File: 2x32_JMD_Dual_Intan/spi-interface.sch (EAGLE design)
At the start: 40 parts, among them Q1 BC817, Q2 BC817

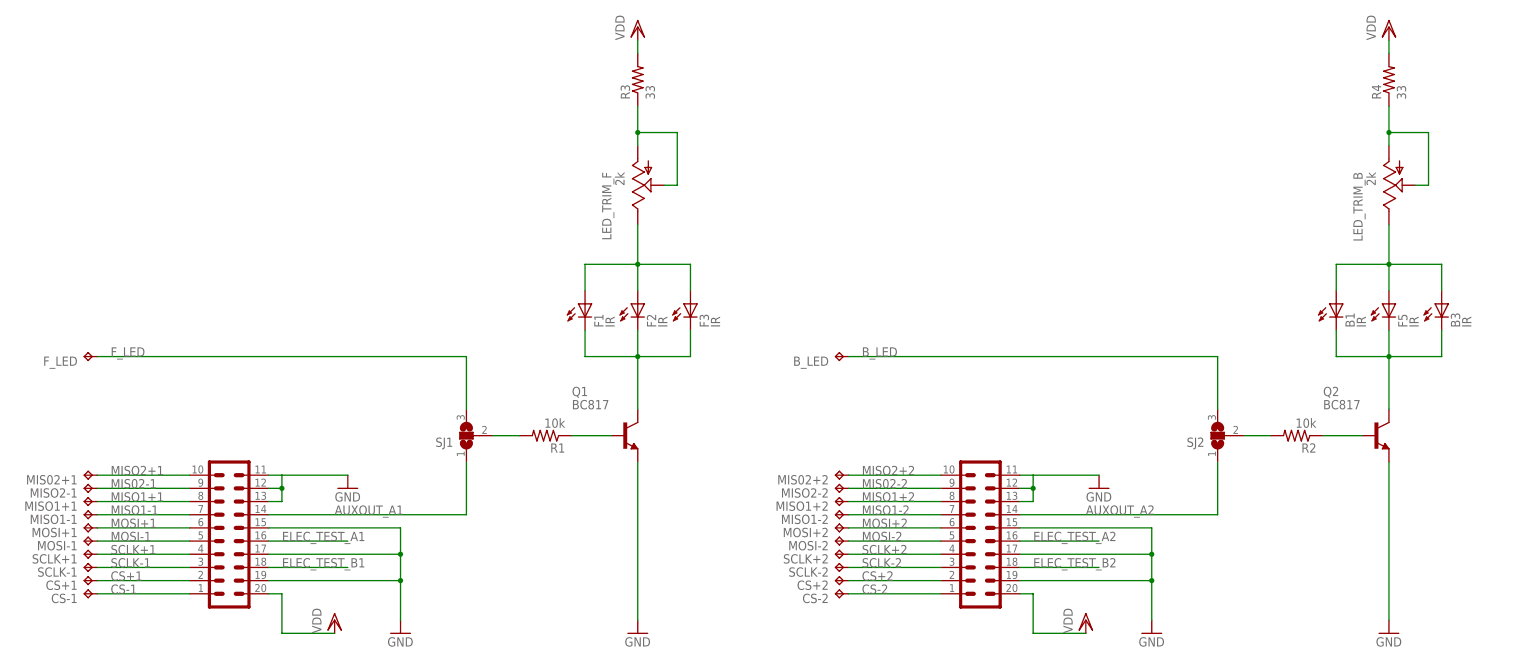
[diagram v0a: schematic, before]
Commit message: Should be finished with JMD spi cable interface. I'm going to wait a day before fabricating.
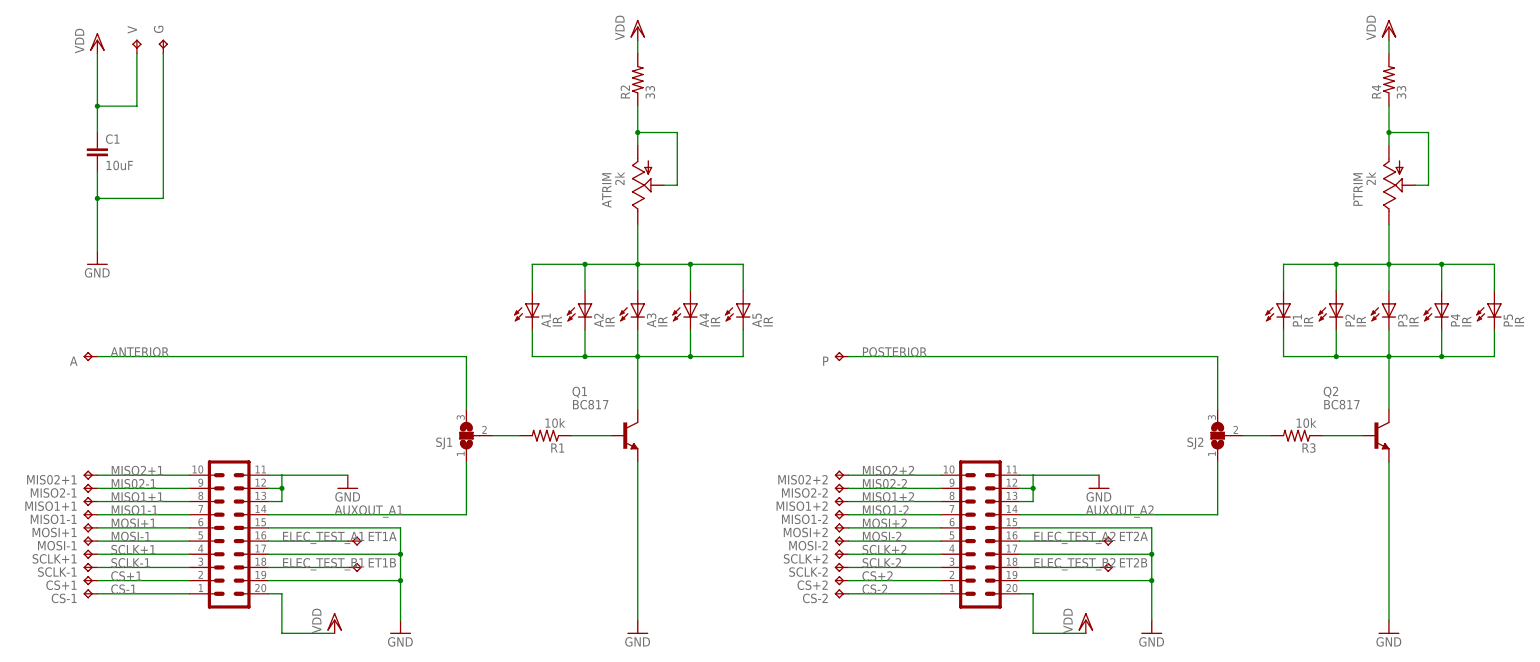
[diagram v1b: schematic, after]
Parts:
- added A1, A5, P1, P5: IR, cyclops:LED_0603
- added C1: 10uF, headstage:C_0805
- added ET1A, ET1B, ET2A, ET2B: TP_03, headstage:TP_03
- added G, V: TP_02, headstage:TP_02
- R2: value 10k -> 33
- R3: value 33 -> 10k
- renumbered B1 to P2, B3 to P4, B_LED to P, F1 to A2, F2 to A3, F3 to A4, F5 to P3, F_LED to A, LED_TRIM_B to PTRIM, LED_TRIM_F to ATRIM
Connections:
- net B_LED renamed POSTERIOR
- net F_LED renamed ANTERIOR
- net B2: now also P1.C, P5.C
- net ELEC_TEST_A1: now also ET1A.TP
- net ELEC_TEST_A2: now also ET2A.TP
- net ELEC_TEST_B1: now also ET1B.TP
- net ELEC_TEST_B2: now also ET2B.TP
- net F1: now also A1.C, A5.C
- net GND: now also C1.2, G.TP
- net N$1: now also A1.A, A5.A
- net N$2: now also R2.1; no longer R3.1
- net N$4: now also R3.2; no longer R2.2
- net N$5: now also R3.1; no longer R2.1
- net N$6: now also P1.A, P5.A
- net VDD: now also C1.1, R2.2, V.TP; no longer R3.2
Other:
- moved on the sheet: R2, R3

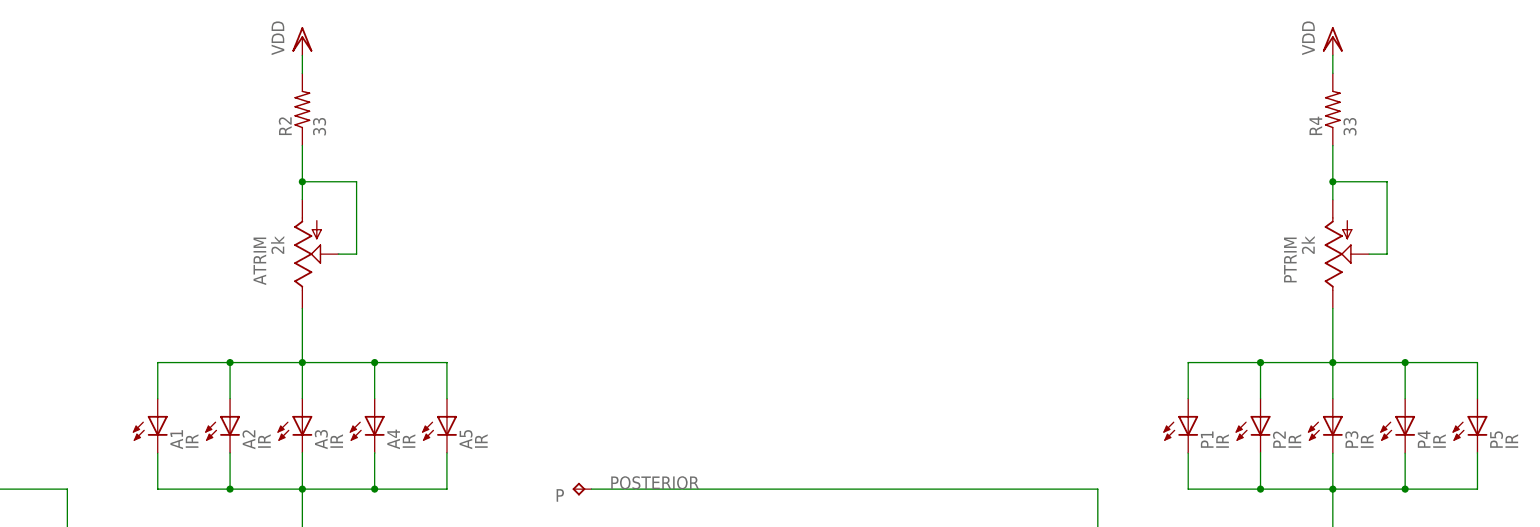
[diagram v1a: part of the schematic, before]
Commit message: Changed LED current limit scheme on JMD spi interface.
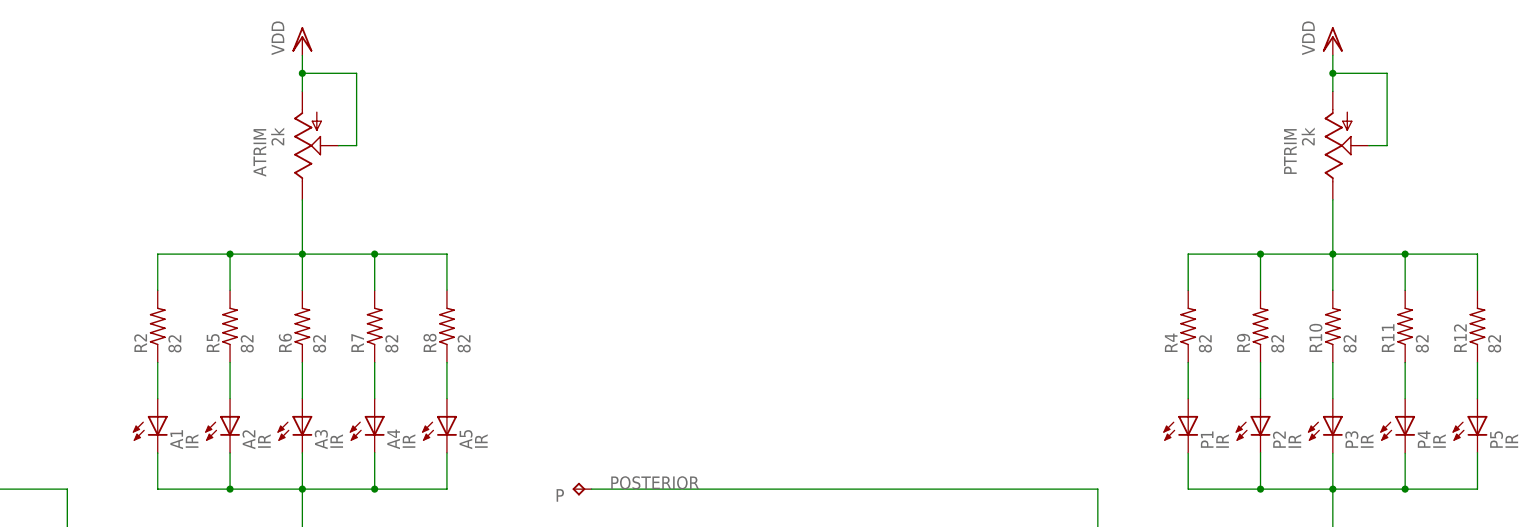
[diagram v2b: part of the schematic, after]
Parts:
- added R10, R11, R12, R5, R6, R7, R8, R9: 82, headstage:R_0402
- HS1, HS2: value PINHD-2X10_JMD20-V -> JMD20-V
- R2, R4: value 33 -> 82
- renumbered HEADSTAGE_1 to HS1, HEADSTAGE_2 to HS2
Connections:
- removed net N$7: PTRIM.A, PTRIM.S, R4.1
- new net N$10: A4.A, R7.1
- new net N$11: A5.A, R8.1
- new net N$12: P2.A, R9.1
- new net N$13: P3.A, R10.1
- new net N$14: P4.A, R11.1
- new net N$15: P5.A, R12.1
- new net N$3: A1.A, R2.1
- new net N$8: A2.A, R5.1
- new net N$9: A3.A, R6.1
- net N$1: now also R2.2, R5.2, R6.2, R7.2, R8.2; no longer A1.A, A2.A, A3.A, A4.A, A5.A
- net N$2: now also P1.A, R4.1; no longer ATRIM.A, ATRIM.S, R2.1
- net N$6: now also R10.2, R11.2, R12.2, R4.2, R9.2; no longer P1.A, P2.A, P3.A, P4.A, P5.A
- net VDD: now also ATRIM.A, ATRIM.S, PTRIM.A, PTRIM.S; no longer R2.2, R4.2
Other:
- moved on the sheet: ATRIM, PTRIM, R2, R4

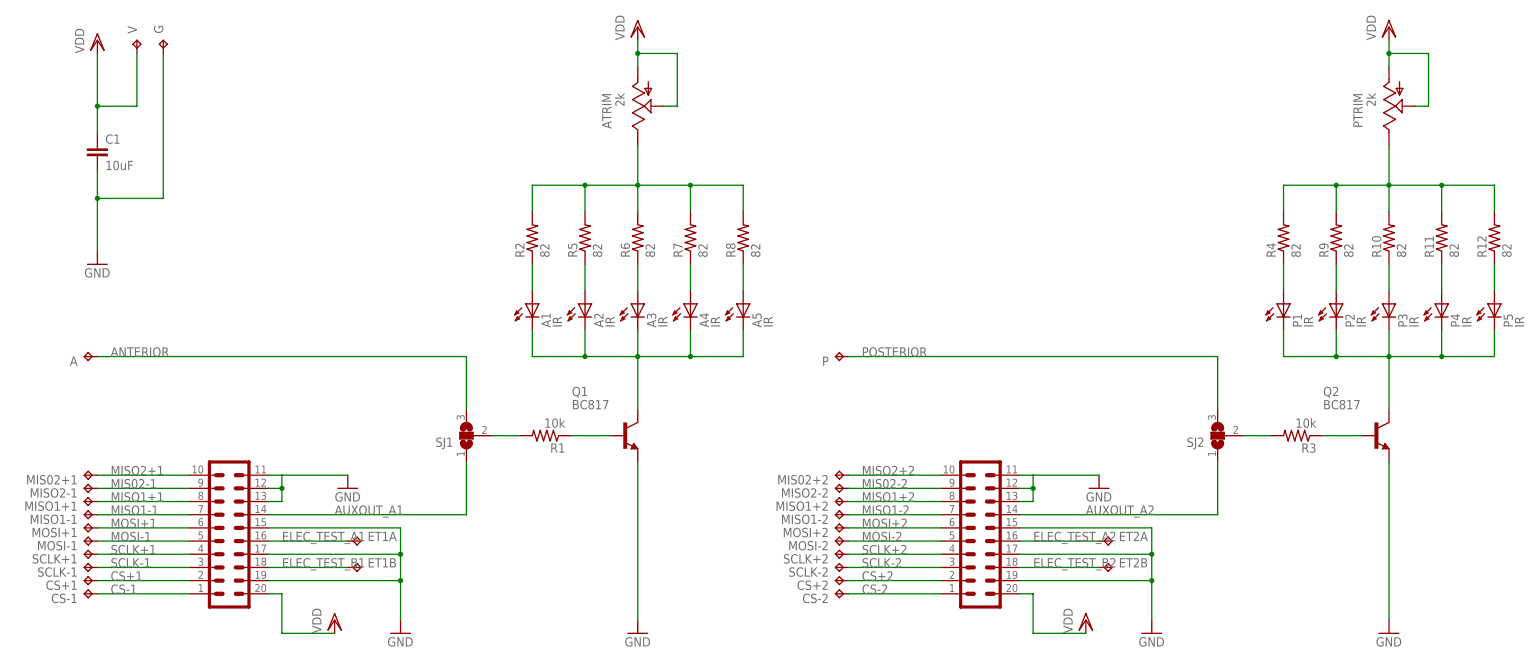
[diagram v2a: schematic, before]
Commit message: Finished the JMD SPI interface board.
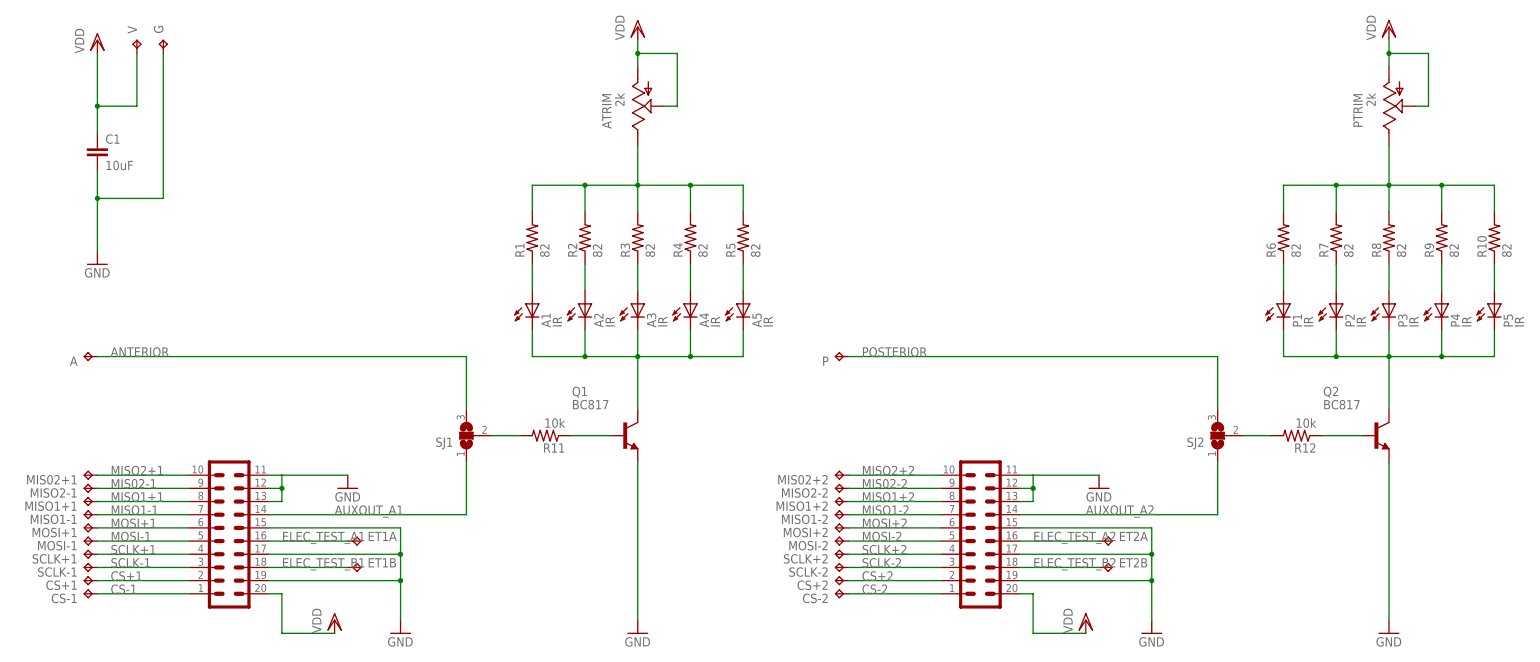
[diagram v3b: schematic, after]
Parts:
- R1, R3: value 10k -> 82
- R11, R12: value 82 -> 10k
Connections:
- net N$1: now also R1.2, R3.2, R4.2; no longer R6.2, R7.2, R8.2
- net N$10: now also R4.1; no longer R7.1
- net N$11: now also R5.1; no longer R8.1
- net N$12: now also R7.1; no longer R9.1
- net N$13: now also R8.1; no longer R10.1
- net N$14: now also R9.1; no longer R11.1
- net N$15: now also R10.1; no longer R12.1
- net N$2: now also R6.1; no longer R4.1
- net N$28: now also R11.1; no longer R1.1
- net N$3: now also R1.1; no longer R2.1
- net N$34: now also R11.2; no longer R1.2
- net N$4: now also R12.2; no longer R3.2
- net N$5: now also R12.1; no longer R3.1
- net N$6: now also R6.2, R7.2, R8.2; no longer R11.2, R12.2, R4.2
- net N$8: now also R2.1; no longer R5.1
- net N$9: now also R3.1; no longer R6.1
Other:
- moved on the sheet: R1, R10, R11, R12, R2, R3, R4, R5, R6, R7, R8, R9
